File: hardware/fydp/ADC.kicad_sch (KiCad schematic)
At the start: 22 parts, among them U53 LTC2353ILX-16-PBF

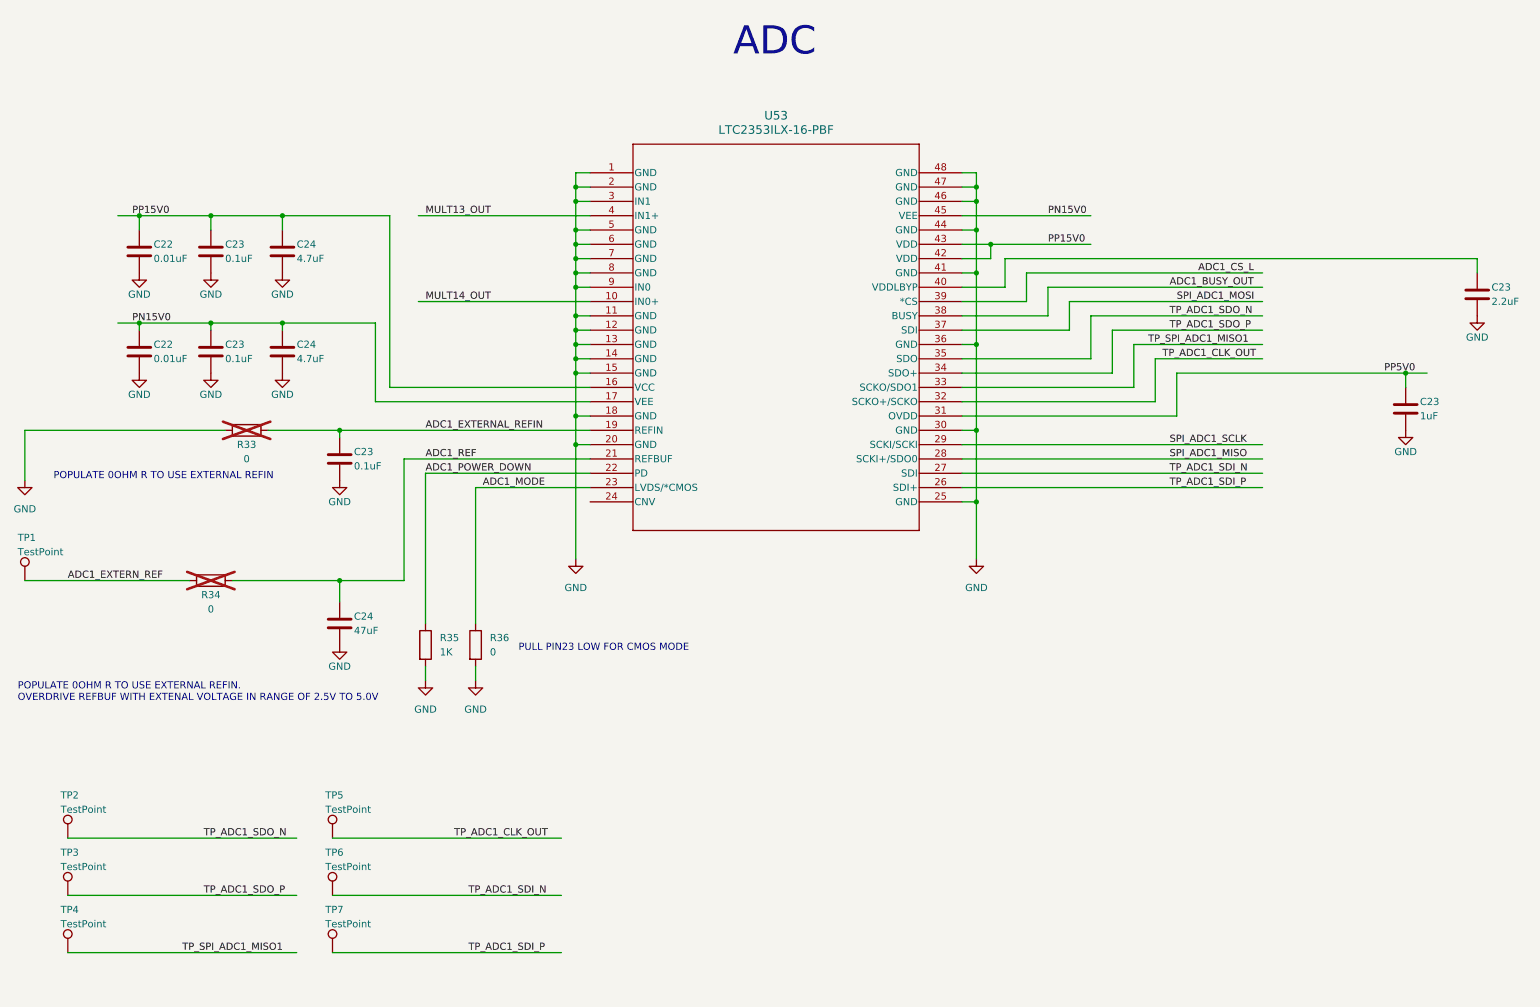
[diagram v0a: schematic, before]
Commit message: Remove 2 channels of multiplier and change ADC
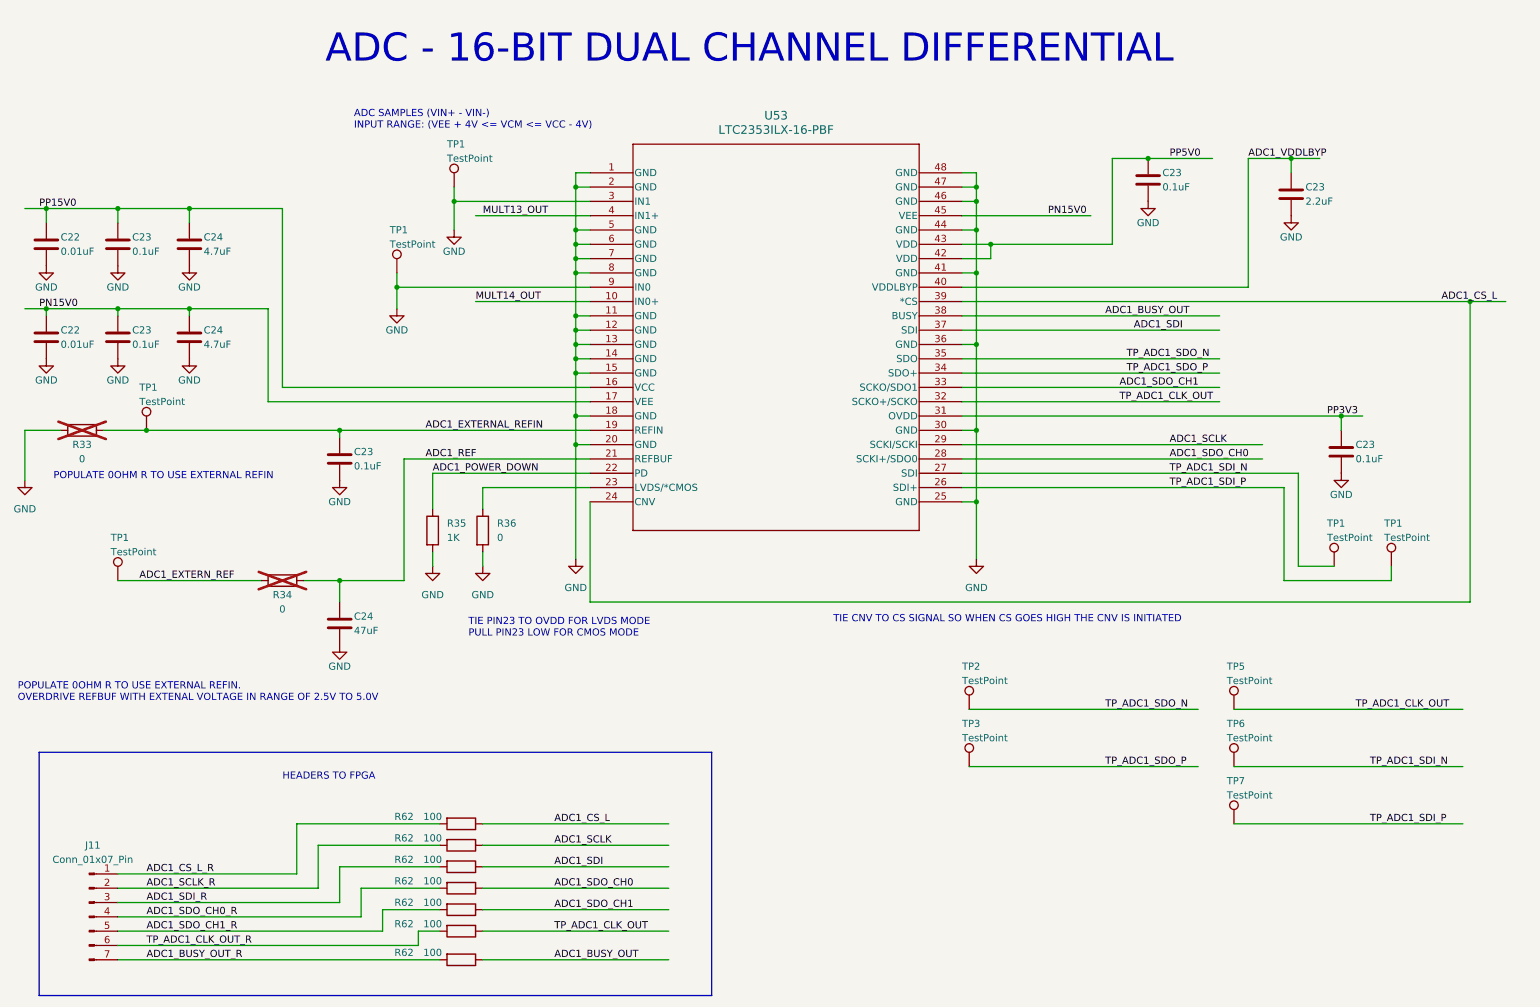
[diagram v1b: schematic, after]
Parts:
- removed TP4: TestPoint, TestPoint:TestPoint_Pad_1.0x1.0mm, symbol Connector:TestPoint
- added C23: 0.1uF, Capacitor_SMD:C_0805_2012Metric, symbol Device:C
- added J11: Conn_01x07_Pin, symbol Connector:Conn_01x07_Pin
- added R62 (x7): 100, Resistor_SMD:R_0805_2012Metric, symbol Device:R
- added TP1 (x5): TestPoint, TestPoint:TestPoint_Pad_1.0x1.0mm, symbol Connector:TestPoint
- C23: value 1uF -> 0.1uF
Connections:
- net ADC1_BUSY_OUT: now also R62.1
- net ADC1_CS_L: now also U53.24 (CNV), R62.1
- net ADC1_EXTERNAL_REFIN: now also TP1.1
- net GND: now also C23.2, TP1.1, TP1.1
- net PP15V0: no longer U53.42 (VDD), U53.43 (VDD)
- net PP5V0: now also U53.42 (VDD), U53.43 (VDD), C23.1; no longer C23.1, U53.31 (OVDD)
- net TP_ADC1_CLK_OUT: now also R62.1
- net TP_ADC1_SDI_N: now also TP1.1
- net TP_ADC1_SDI_P: now also TP1.1
- net ADC1_VDDLBYP: now reaches C23.1, U53.40 (VDDLBYP)
- net ADC1_MODE: no longer names the net of R36.1, U53.23 (LVDS/*CMOS)
- net SPI_ADC1_MISO renamed ADC1_SDO_CH0
- net ADC1_SDO_CH0: now also R62.1
- net SPI_ADC1_MOSI renamed ADC1_SDI
- net ADC1_SDI: now also R62.1
- net SPI_ADC1_SCLK renamed ADC1_SCLK
- net ADC1_SCLK: now also R62.1
- net TP_SPI_ADC1_MISO1 renamed ADC1_SDO_CH1
- net ADC1_SDO_CH1: now also R62.1
- new net ADC1_BUSY_OUT_R: J11.7 (Pin_7), R62.2
- new net ADC1_CS_L_R: J11.1 (Pin_1), R62.2
- new net ADC1_SCLK_R: J11.2 (Pin_2), R62.2
- new net ADC1_SDI_R: J11.3 (Pin_3), R62.2
- new net ADC1_SDO_CH0_R: J11.4 (Pin_4), R62.2
- new net ADC1_SDO_CH1_R: J11.5 (Pin_5), R62.2
- new net PP3V3: C23.1, U53.31 (OVDD)
- new net TP_ADC1_CLK_OUT_R: J11.6 (Pin_6), R62.2
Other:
- note added: "ADC - 16-BIT DUAL CHANNEL DIFFERENTIAL"
- note added: "ADC SAMPLES (VIN+ - VIN-) INPUT RANGE: (VEE + 4V <= VCM <= VCC - 4V)"
- note added: "HEADERS TO FPGA"
- note added: "TIE CNV TO CS SIGNAL SO WHEN CS GOES HIGH THE CNV IS INITIATED"
- note added: "TIE PIN23 TO OVDD FOR LVDS MODE PULL PIN23 LOW FOR CMOS MODE"
- note removed: "ADC"
- note removed: "PULL PIN23 LOW FOR CMOS MODE"
- moved on the sheet: C22, C23, C24, R33, R34, R35, R36, TP1, TP2, TP3, TP5, TP6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

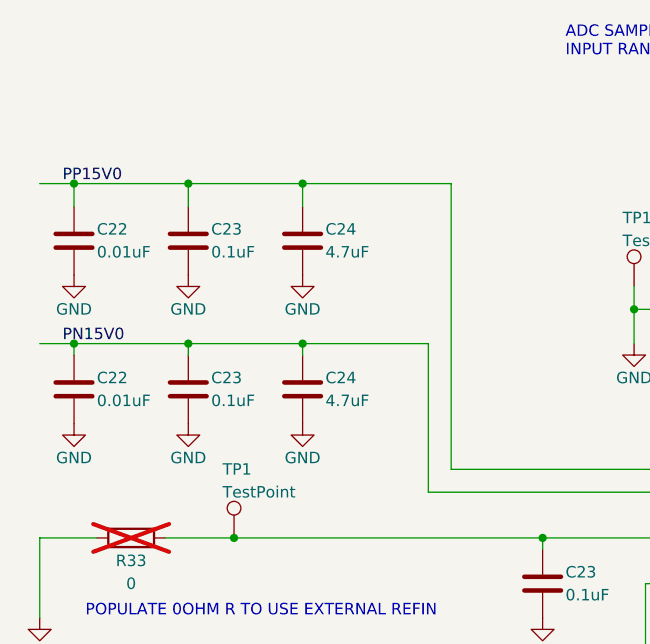
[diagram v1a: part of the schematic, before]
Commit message: remove caps on VDD and VEE on ADC
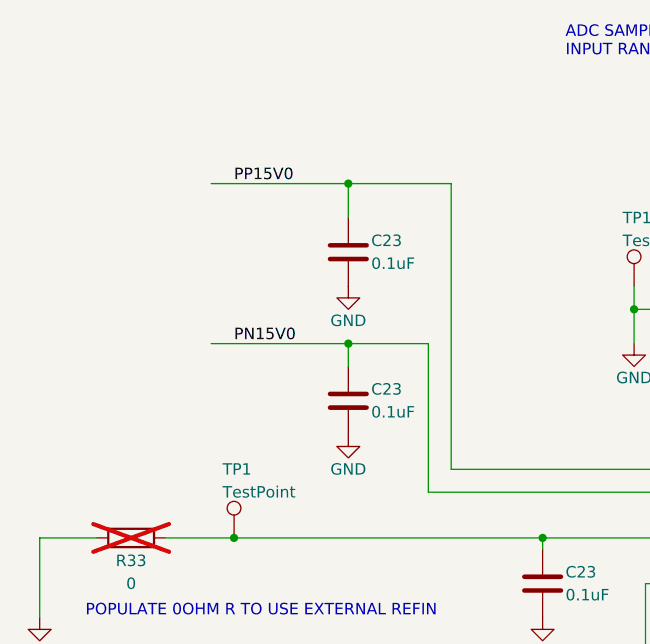
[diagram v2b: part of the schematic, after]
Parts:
- removed C22 (x2): 0.01uF, Capacitor_SMD:C_0805_2012Metric, symbol Device:C
- removed C24 (x2): 4.7uF, Capacitor_SMD:C_0805_2012Metric, symbol Device:C
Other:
- moved on the sheet: C23

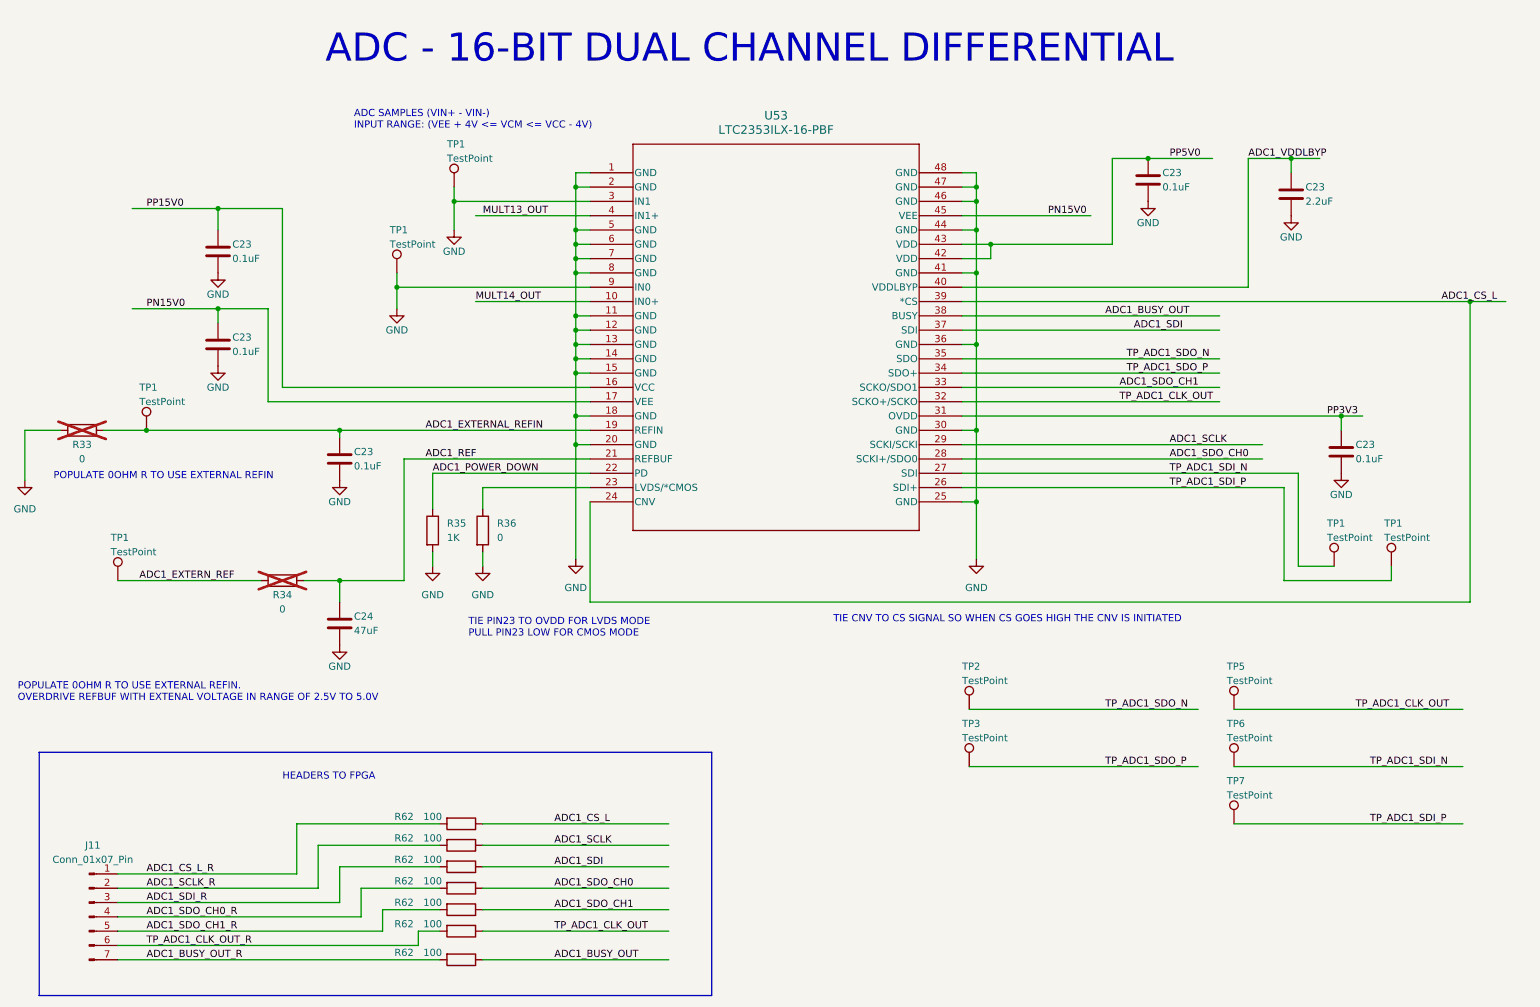
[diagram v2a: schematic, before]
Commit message: Initial layout mostly complete, need to complete lots of routing
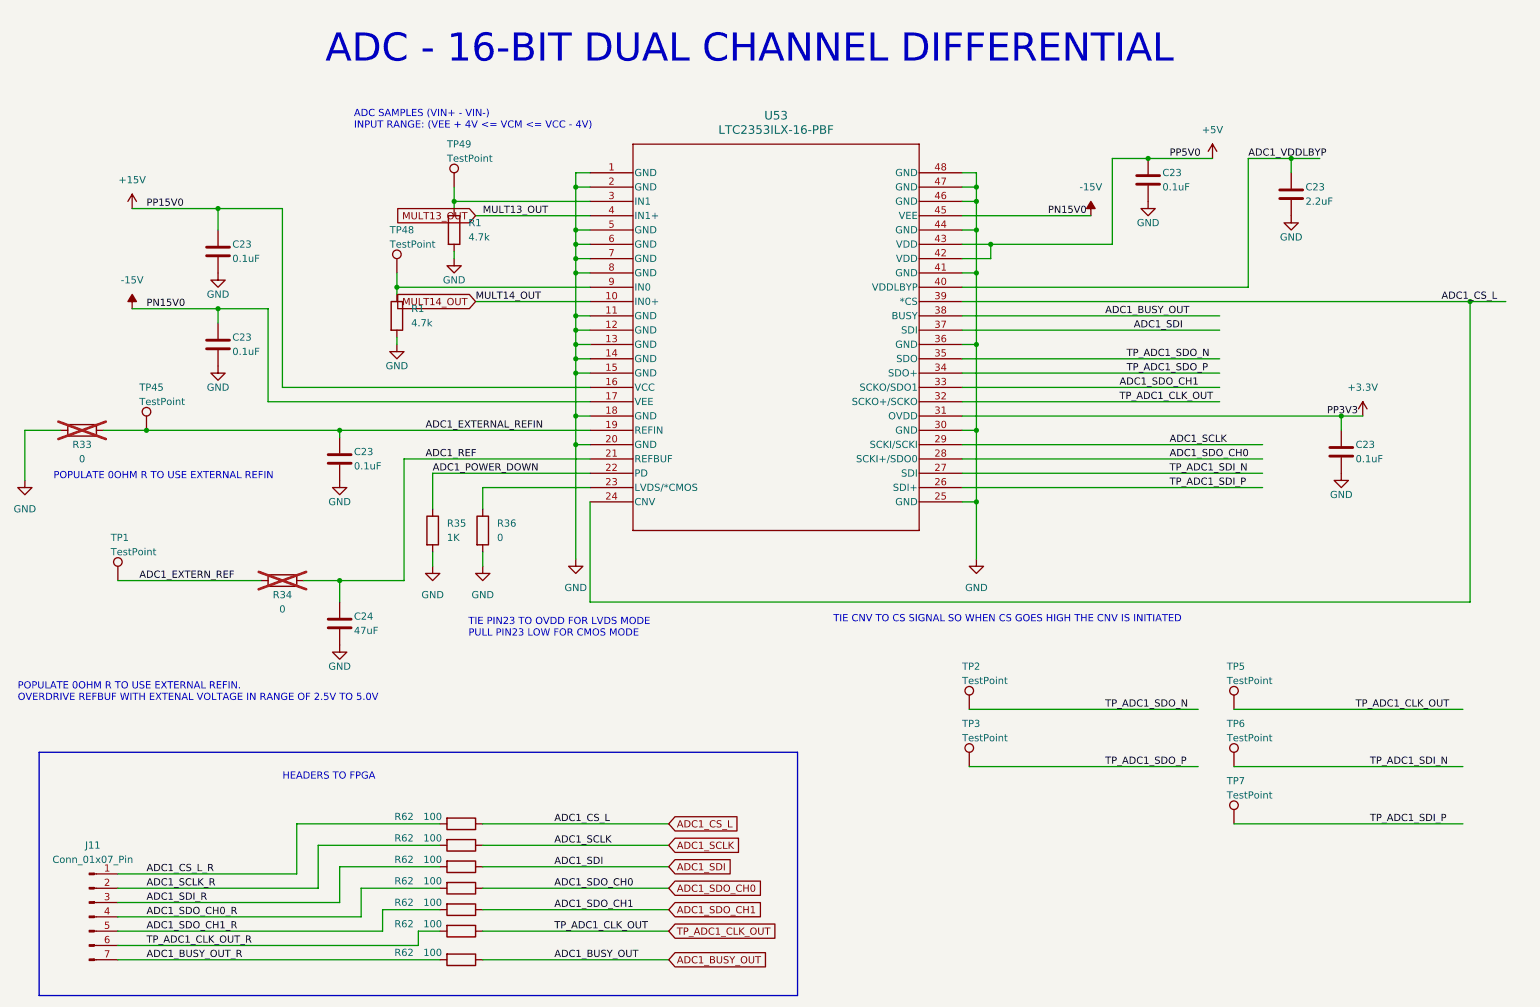
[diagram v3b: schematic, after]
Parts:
- removed C23 (x4): 0.1uF, Capacitor_SMD:C_0805_2012Metric, symbol Device:C
- removed C23: 2.2uF, Capacitor_SMD:C_0805_2012Metric, symbol Device:C
- removed TP1 (x2): TestPoint, TestPoint:TestPoint_Pad_1.0x1.0mm, symbol Connector:TestPoint
- added C23 (x4): 0.1uF, Capacitor_SMD:C_0805_2012Metric, symbol Device:C
- added C23: 2.2uF, Capacitor_SMD:C_0805_2012Metric, symbol Device:C
- added R1 (x2): 4.7k, Resistor_SMD:R_0805_2012Metric, symbol Device:R
- J11: footprint (none) -> Connector_PinHeader_2.54mm:PinHeader_1x07_P2.54mm_Vertical
- U53: footprint QFP_48_ADI -> Package_QFP:LQFP-48_7x7mm_P0.5mm
- renumbered TP1 to TP45, TP1 to TP48, TP1 to TP49
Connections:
- net ADC1_EXTERNAL_REFIN: now also C23.1
- net ADC1_VDDLBYP: now also C23.1
- net GND: now also C23.2, C23.2, C23.2, C23.2, C23.2, R1.2, R1.2; no longer TP48.1, TP49.1, U53.3 (IN1), U53.9 (IN0)
- net PN15V0 renamed -15V
- net -15V: now also C23.1
- net PP15V0 renamed +15V
- net +15V: now also C23.1
- net PP3V3 renamed +3.3V
- net +3.3V: now also C23.1
- net PP5V0 renamed +5V
- new net: R1.1, TP48.1, U53.9 (IN0)
- new net: R1.1, TP49.1, U53.3 (IN1)

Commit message: Completed placement and silk for left and centre sections of the PCB
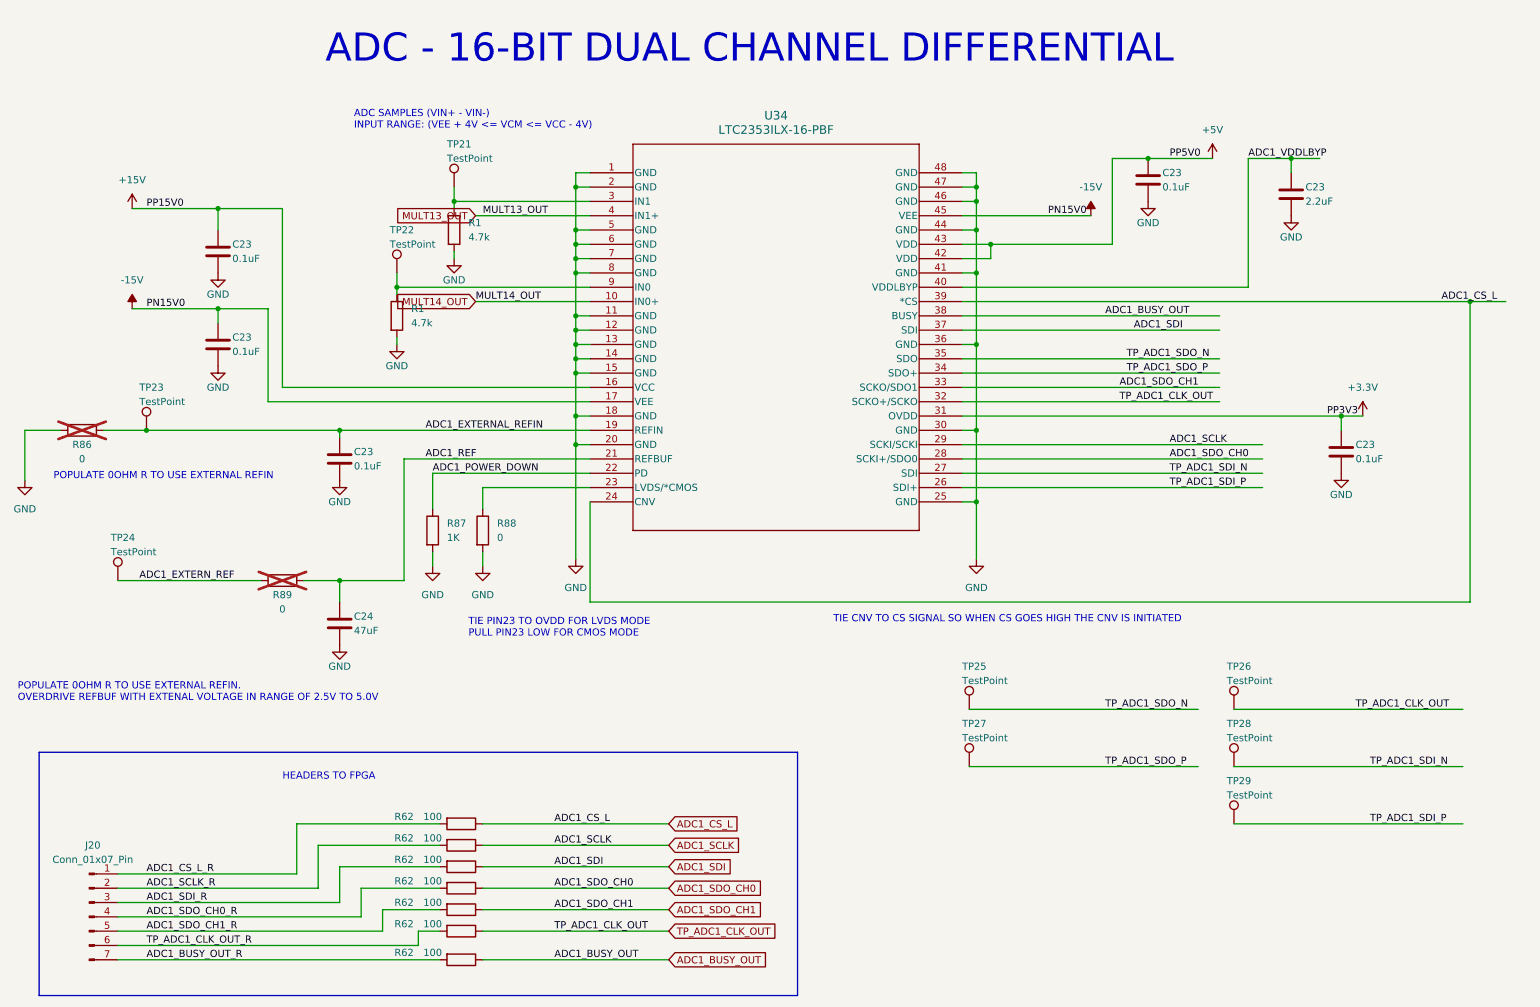
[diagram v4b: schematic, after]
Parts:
- renumbered J11 to J20, R33 to R86, R35 to R87, R36 to R88, R34 to R89, TP49 to TP21, TP48 to TP22, TP45 to TP23, TP1 to TP24, TP2 to TP25, TP5 to TP26, TP3 to TP27, TP6 to TP28, TP7 to TP29, U53 to U34

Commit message: Pushing all changes, I'm late for class
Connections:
- net IN0: now reaches R1.1, TP22.1, U34.9 (IN0)
- net IN1: now reaches R1.1, TP21.1, U34.3 (IN1)
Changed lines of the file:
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@@
     (effects (font (size 1.27 1.27)) (justify left bottom))
   )
-  (label "MULT14_OUT" (at 96.52 67.31 0) (fields_autoplaced)
+  (label "MULT14_OUT" (at 97.79 67.31 0) (fields_autoplaced)
     (effects (font (size 1.27 1.27)) (justify left bottom))
   )
@@
     (effects (font (size 1.27 1.27)) (justify left bottom))
   )
+  (label "IN1" (at 97.79 49.53 0) (fields_autoplaced)
+    (effects (font (size 1.27 1.27)) (justify left bottom))
+  )
   (label "ADC1_VDDLBYP" (at 233.68 41.91 0) (fields_autoplaced)
     (effects (font (size 1.27 1.27)) (justify left bottom))
@@
     (effects (font (size 1.27 1.27)) (justify left bottom))
   )
+  (label "IN0" (at 97.79 64.77 0) (fields_autoplaced)
+    (effects (font (size 1.27 1.27)) (justify left bottom))
+  )
